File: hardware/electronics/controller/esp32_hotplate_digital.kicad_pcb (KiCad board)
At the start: 2 copper layers, 89.1 x 49.4 mm, 87 parts, among them IC1 ADC081S021CIMF_NOPB, IC2 ADC081S021CIMF_NOPB, J2 JST XH, J3 JST XH, J4 JST XH, J5 JST XH, J6 USB_B_Micro, J7 JST XH, J8 105162-0001, J9 Conn_01x04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

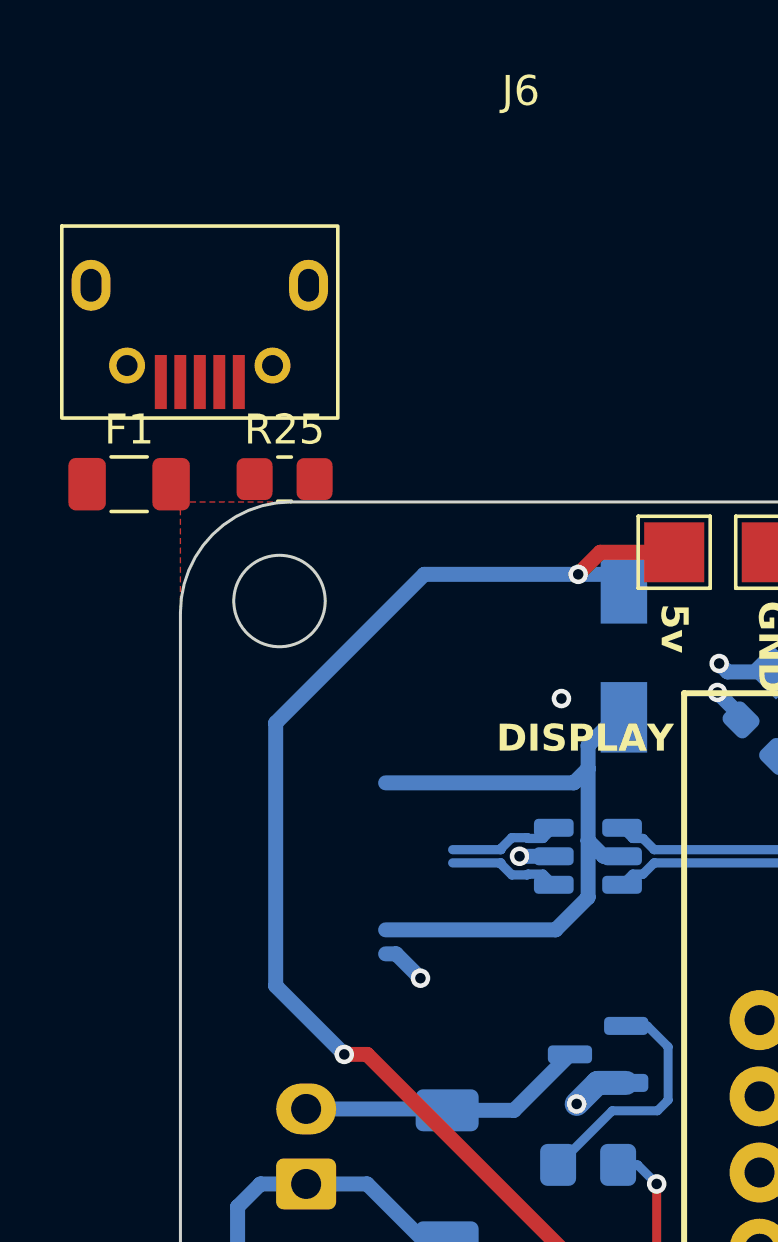
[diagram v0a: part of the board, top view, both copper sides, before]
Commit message: attempting to get the sd card working with SPI
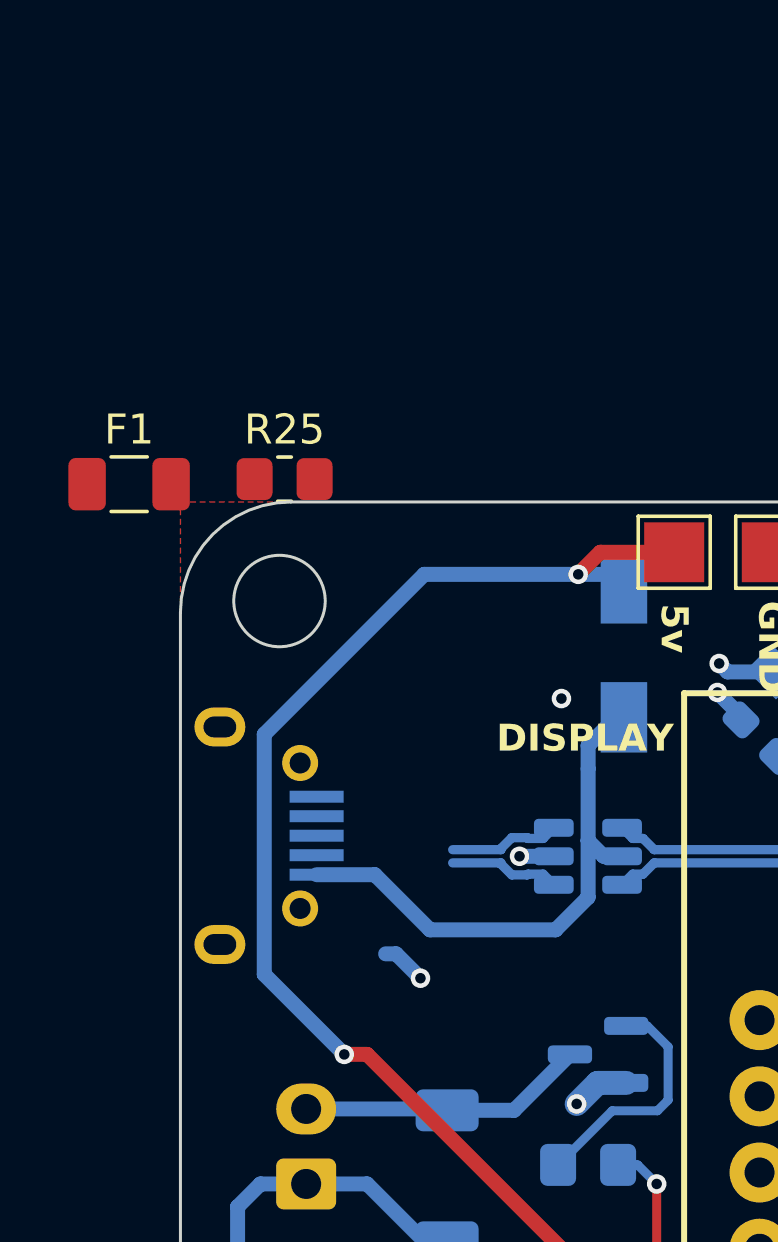
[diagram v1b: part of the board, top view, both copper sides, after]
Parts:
- J6: moved to B.Cu
- moved J6 17.1 mm to (46.2, 62.4), turned to -90 degrees
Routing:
- net VBUS: track 22.0 -> 18.1 mm
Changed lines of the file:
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@@
     )
   )
-  (footprint "Connector_USB:microXNJ" (layer "F.Cu")
-    (at 44.0794 45.511)
-    (property "Sheetfile" "esp32_hotplate_digital.kicad_sch")
-    (property "Sheetname" "")
-    (property "ki_description" "USB Micro Type B connector")
-    (property "ki_keywords" "connector USB micro")
-    (fp_text reference "J6" (at 10.7 -7.9 unlocked) (layer "F.SilkS")
-        (effects (font (size 1 1) (thickness 0.15)))
-    )
-    (fp_text value "USB_B_Micro" (at 10.7 -6.4 unlocked) (layer "F.Fab")
-        (effects (font (size 1 1) (thickness 0.15)))
-    )
-    (fp_text user "${REFERENCE}" (at 10.7 -4.9 unlocked) (layer "F.Fab")
-        (effects (font (size 1 1) (thickness 0.15)))
-    )
-    (fp_rect (start -4.6 -3.4) (end 4.6 3)
-      (stroke (width 0.12) (type default)) (fill none) (layer "F.SilkS"))
-    (fp_rect (start -4.6 -3.4) (end 4.6 3)
-      (stroke (width 0.05) (type default)) (fill none) (layer "F.CrtYd"))
-    (pad "1" smd rect (at 1.3 1.8) (size 0.4 1.8) (layers "F.Cu" "F.Paste" "F.Mask")
-      (net 21 "VBUS") (pinfunction "VBUS") (pintype "power_out"))
-    (pad "2" smd rect (at 0.65 1.8) (size 0.4 1.8) (layers "F.Cu" "F.Paste" "F.Mask")
-      (net 23 "/usb_D-") (pinfunction "D-") (pintype "bidirectional"))
-    (pad "3" smd rect (at 0 1.8) (size 0.4 1.8) (layers "F.Cu" "F.Paste" "F.Mask")
-      (net 22 "/usb_D+") (pinfunction "D+") (pintype "bidirectional"))
-    (pad "4" smd rect (at -0.65 1.8) (size 0.4 1.8) (layers "F.Cu" "F.Paste" "F.Mask")
-      (net 79 "unconnected-(J6-ID-Pad4)") (pinfunction "ID") (pintype "passive"))
-    (pad "5" smd rect (at -1.3 1.8) (size 0.4 1.8) (layers "F.Cu" "F.Paste" "F.Mask")
-      (net 4 "GND") (pinfunction "GND") (pintype "power_out"))
-    (pad "6" thru_hole oval (at -3.625 -1.425) (size 1.3 1.7) (drill oval 0.7 1.1) (layers "*.Cu" "*.Mask")
-      (net 4 "GND") (pinfunction "Shield") (pintype "passive"))
-    (pad "6" thru_hole circle (at -2.425 1.25) (size 1.2 1.2) (drill 0.7) (layers "*.Cu" "*.Mask")
-      (net 4 "GND") (pinfunction "Shield") (pintype "passive"))
-    (pad "6" thru_hole circle (at 2.425 1.25) (size 1.2 1.2) (drill 0.7) (layers "*.Cu" "*.Mask")
-      (net 4 "GND") (pinfunction "Shield") (pintype "passive"))
-    (pad "6" thru_hole oval (at 3.625 -1.425) (size 1.3 1.7) (drill oval 0.7 1.1) (layers "*.Cu" "*.Mask")
-      (net 4 "GND") (pinfunction "Shield") (pintype "passive"))
-  )
   (footprint "TestPoint:TestPoint_Pad_2.0x2.0mm" locked (layer "F.Cu")
     (at 68.58 52.9844 180)
@@
     )
   )
+  (footprint "Connector_USB:microXNJ" (layer "B.Cu")
+    (at 46.173999 62.4332 -90)
+    (property "Sheetfile" "esp32_hotplate_digital.kicad_sch")
+    (property "Sheetname" "")
+    (property "ki_description" "USB Micro Type B connector")
+    (property "ki_keywords" "connector USB micro")
+    (fp_text reference "J6" (at -0.0358 2.4326 90 unlocked) (layer "B.SilkS")
+        (effects (font (size 1 1) (thickness 0.15)) (justify mirror))
+    )
+    (fp_text value "USB_B_Micro" (at 10.7 6.4 90 unlocked) (layer "B.Fab")
+        (effects (font (size 1 1) (thickness 0.15)) (justify mirror))
+    )
+    (fp_text user "${REFERENCE}" (at 10.7 4.9 90 unlocked) (layer "B.Fab")
+        (effects (font (size 1 1) (thickness 0.15)) (justify mirror))
+    )
+    (fp_rect (start -4.6 3.4) (end 4.6 -3)
+      (stroke (width 0.12) (type default)) (fill none) (layer "B.SilkS"))
+    (fp_rect (start -4.6 3.4) (end 4.6 -3)
+      (stroke (width 0.05) (type default)) (fill none) (layer "B.CrtYd"))
+    (pad "1" smd rect (at 1.3 -1.8 270) (size 0.4 1.8) (layers "B.Cu" "B.Paste" "B.Mask")
+      (net 21 "VBUS") (pinfunction "VBUS") (pintype "power_out"))
+    (pad "2" smd rect (at 0.65 -1.8 270) (size 0.4 1.8) (layers "B.Cu" "B.Paste" "B.Mask")
+      (net 23 "/usb_D-") (pinfunction "D-") (pintype "bidirectional"))
+    (pad "3" smd rect (at 0 -1.8 270) (size 0.4 1.8) (layers "B.Cu" "B.Paste" "B.Mask")
+      (net 22 "/usb_D+") (pinfunction "D+") (pintype "bidirectional"))
+    (pad "4" smd rect (at -0.65 -1.8 270) (size 0.4 1.8) (layers "B.Cu" "B.Paste" "B.Mask")
+      (net 79 "unconnected-(J6-ID-Pad4)") (pinfunction "ID") (pintype "passive"))
+    (pad "5" smd rect (at -1.3 -1.8 270) (size 0.4 1.8) (layers "B.Cu" "B.Paste" "B.Mask")
+      (net 4 "GND") (pinfunction "GND") (pintype "power_out"))
+    (pad "6" thru_hole oval (at -3.625 1.425 270) (size 1.3 1.7) (drill oval 0.7 1.1) (layers "*.Cu" "*.Mask")
+      (net 4 "GND") (pinfunction "Shield") (pintype "passive"))
+    (pad "6" thru_hole circle (at -2.425 -1.25 270) (size 1.2 1.2) (drill 0.7) (layers "*.Cu" "*.Mask")
+      (net 4 "GND") (pinfunction "Shield") (pintype "passive"))
+    (pad "6" thru_hole circle (at 2.425 -1.25 270) (size 1.2 1.2) (drill 0.7) (layers "*.Cu" "*.Mask")
+      (net 4 "GND") (pinfunction "Shield") (pintype "passive"))
+    (pad "6" thru_hole oval (at 3.625 1.425 270) (size 1.3 1.7) (drill oval 0.7 1.1) (layers "*.Cu" "*.Mask")
+      (net 4 "GND") (pinfunction "Shield") (pintype "passive"))
+    (model ":KICAD7_3DMODEL_DIR:Connector_USB.3dshapes/USB_Micro-B_Molex_47346-0001.wrl"
+      (offset (xyz 0 0 0))
+      (scale (xyz 1 1 1))
+      (rotate (xyz 0 0 180))
+    )
+  )
   (footprint "Resistor_SMD:R_0805_2012Metric_Pad1.20x1.40mm_HandSolder" (layer "B.Cu")
     (at 57.404 85.598)
@@
   (via (at 48.895 69.723) (size 0.65) (drill 0.35) (layers "F.Cu" "B.Cu") (net 7))
   (via (at 56.6928 53.721) (size 0.65) (drill 0.35) (layers "F.Cu" "B.Cu") (net 7))
-  (segment (start 46.609 58.674) (end 51.562 53.721) (width 0.5) (layer "B.Cu") (net 7))
+  (segment (start 46.228 67.056) (end 46.228 59.055) (width 0.5) (layer "B.Cu") (net 7))
   (segment (start 70.299 97.858) (end 94.912001 97.858) (width 0.5) (layer "B.Cu") (net 7))
   (segment (start 98.790001 93.710001) (end 97.536 92.456) (width 0.5) (layer "B.Cu") (net 7))
   (segment (start 99.06 93.710001) (end 98.790001 93.710001) (width 0.5) (layer "B.Cu") (net 7))
-  (segment (start 46.609 67.437) (end 46.609 58.674) (width 0.5) (layer "B.Cu") (net 7))
   (segment (start 97.536 85.8905) (end 96.4815 84.836) (width 0.5) (layer "B.Cu") (net 7))
   (segment (start 96.4815 84.836) (end 99.2615 82.056) (width 0.5) (layer "B.Cu") (net 7))
+  (segment (start 46.228 59.055) (end 51.562 53.721) (width 0.5) (layer "B.Cu") (net 7))
   (segment (start 56.6928 53.721) (end 57.649 53.721) (width 0.5) (layer "B.Cu") (net 7))
   (segment (start 57.649 53.721) (end 58.039 54.111) (width 0.5) (layer "B.Cu") (net 7))
+  (segment (start 48.895 69.723) (end 46.228 67.056) (width 0.5) (layer "B.Cu") (net 7))
   (segment (start 66.0815 97.075) (end 64.7315 98.425) (width 0.5) (layer "B.Cu") (net 7))
   (segment (start 99.2615 82.056) (end 102.972 82.056) (width 0.5) (layer "B.Cu") (net 7))
   (segment (start 103.6535 82.7375) (end 102.972 82.056) (width 0.5) (layer "B.Cu") (net 7))
   (segment (start 64.659 91.59867) (end 64.659 95.758) (width 0.5) (layer "B.Cu") (net 7))
-  (segment (start 51.562 53.721) (end 56.6928 53.721) (width 0.5) (layer "B.Cu") (net 7))
   (segment (start 69.215 97.075) (end 69.516 97.075) (width 0.5) (layer "B.Cu") (net 7))
-  (segment (start 48.895 69.723) (end 46.609 67.437) (width 0.5) (layer "B.Cu") (net 7))
   (segment (start 97.536 92.456) (end 97.536 85.8905) (width 0.5) (layer "B.Cu") (net 7))
   (segment (start 64.381165 91.320835) (end 64.659 91.59867) (width 0.5) (layer "B.Cu") (net 7))
   (segment (start 69.215 97.075) (end 66.0815 97.075) (width 0.5) (layer "B.Cu") (net 7))
   (segment (start 69.516 97.075) (end 70.299 97.858) (width 0.5) (layer "B.Cu") (net 7))
+  (segment (start 51.562 53.721) (end 56.6928 53.721) (width 0.5) (layer "B.Cu") (net 7))
   (segment (start 103.6535 84.836) (end 103.6535 82.7375) (width 0.5) (layer "B.Cu") (net 7))
   (segment (start 94.912001 97.858) (end 99.06 93.710001) (width 0.5) (layer "B.Cu") (net 7))
@@
   (segment (start 98.407328 68.366) (end 115.916 68.366) (width 0.3) (layer "B.Cu") (net 20))
   (segment (start 73.914 74.676) (end 73.914 73.146) (width 0.3) (layer "B.Cu") (net 20))
-  (segment (start 50.273 60.671) (end 56.55 60.671) (width 0.5) (layer "B.Cu") (net 21))
-  (segment (start 56.55 60.671) (end 57.023 60.198) (width 0.5) (layer "B.Cu") (net 21))
   (segment (start 58.155 63.119) (end 57.543972 63.119) (width 0.5) (layer "B.Cu") (net 21))
   (segment (start 57.023 60.198) (end 57.023 59.427) (width 0.5) (layer "B.Cu") (net 21))
   (segment (start 57.023 59.427) (end 58.039 58.411) (width 0.5) (layer "B.Cu") (net 21))
-  (segment (start 50.273 65.571) (end 55.939028 65.571) (width 0.5) (layer "B.Cu") (net 21))
-  (segment (start 57.023 64.487028) (end 57.023 62.598028) (width 0.5) (layer "B.Cu") (net 21))
+  (segment (start 57.023 62.598028) (end 57.023 64.487028) (width 0.5) (layer "B.Cu") (net 21))
+  (segment (start 57.023 64.487028) (end 55.939028 65.571) (width 0.5) (layer "B.Cu") (net 21))
+  (segment (start 49.9156 63.7332) (end 47.973999 63.7332) (width 0.5) (layer "B.Cu") (net 21))
   (segment (start 57.023 62.598028) (end 57.023 60.198) (width 0.5) (layer "B.Cu") (net 21))
-  (segment (start 55.939028 65.571) (end 57.023 64.487028) (width 0.5) (layer "B.Cu") (net 21))
   (segment (start 57.543972 63.119) (end 57.023 62.598028) (width 0.5) (layer "B.Cu") (net 21))
+  (segment (start 55.939028 65.571) (end 51.7534 65.571) (width 0.5) (layer "B.Cu") (net 21))
+  (segment (start 51.7534 65.571) (end 49.9156 63.7332) (width 0.5) (layer "B.Cu") (net 21))
   (segment (start 54.480187 63.739) (end 54.117 63.375813) (width 0.31) (layer "B.Cu") (net 22))
   (segment (start 54.117 63.375813) (end 54.117 63.339) (width 0.31) (layer "B.Cu") (net 22))

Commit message: fixes for revision2
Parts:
- removed J6: USB_B_Micro, Connector_USB:microXNJ
- added F2: 1A, Fuse:Fuse_1206_3216Metric, F.Cu at (39.6, 94.2)
- added J1: USB_C_Receptacle_USB2.0, Connector_USB:USB_C_Receptacle_HRO_TYPE-C-31-M-12, B.Cu at (46.2, 63.1)
- added R26: 10k, Resistor_SMD:R_0805_2012Metric_Pad1.20x1.40mm_HandSolder, B.Cu at (125.1, 108.4)
- added R27: 10k, Resistor_SMD:R_0805_2012Metric_Pad1.20x1.40mm_HandSolder, B.Cu at (125.1, 111.4)
- added R5: 10k, Resistor_SMD:R_0805_2012Metric_Pad1.20x1.40mm_HandSolder, F.Cu at (17.8, 67.9)
- added R6: 10k, Resistor_SMD:R_0805_2012Metric_Pad1.20x1.40mm_HandSolder, F.Cu at (17.8, 70.9)
- F1: value Fuse -> 1A
- J8: footprint SamacSys_Parts:105162-0001 -> components:TF-SMD_TF-PUSH
- R25: moved to B.Cu
- moved R25 93.9 mm to (116.6, 113.4), turned to 180 degrees
- moved R23 22.7 mm to (109.1, 70.9), turned to -90 degrees
- moved R24 19.1 mm to (111.3, 72.1), turned to -90 degrees
- moved J8 5.20 mm to (122.7, 84.7)
- moved BZ1 2.78 mm to (109.5, 80.4)
- moved R22 2.29 mm to (122.8, 73.5)
- moved R21 1.93 mm to (122.8, 75.6)
- moved R11 1.37 mm to (105.7, 74.5), turned to 0 degrees
- turned SW3 to 0 degrees
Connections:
- J7 pad 2: +12V -> Net-(J7-Pin_2)
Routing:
- net /HSPI_MOSI: track 95.8 -> 70.2 mm
- net /SD_CS: track 92.5 -> 68.1 mm
- net GND: track 87.9 -> 102.9 mm, vias 37 -> 38
- net +3.3V: track 233.1 -> 247.6 mm, vias 5 -> 6
- net /BTN_DOWN: track 66.3 -> 60.8 mm
- net Net-(R10-Pad2): track 60.6 -> 65.7 mm
- net /usb_D-: track 3.72 -> 0.00 mm
- net /usb_D+: track 3.72 -> 0.00 mm
- net VBUS: track 18.1 -> 15.0 mm
- net /HSPI_MISO: track 82.8 -> 80.0 mm
- net /HEATER: track 39.6 -> 41.9 mm
- net /ZERO_CROSS: track 35.5 -> 37.1 mm
- net /HSPI_CLK: track 81.7 -> 83.2 mm
- net /EN: track 54.1 -> 53.5 mm, vias 4 -> 2
- net /DISP_DC: track 27.0 -> 27.5 mm
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
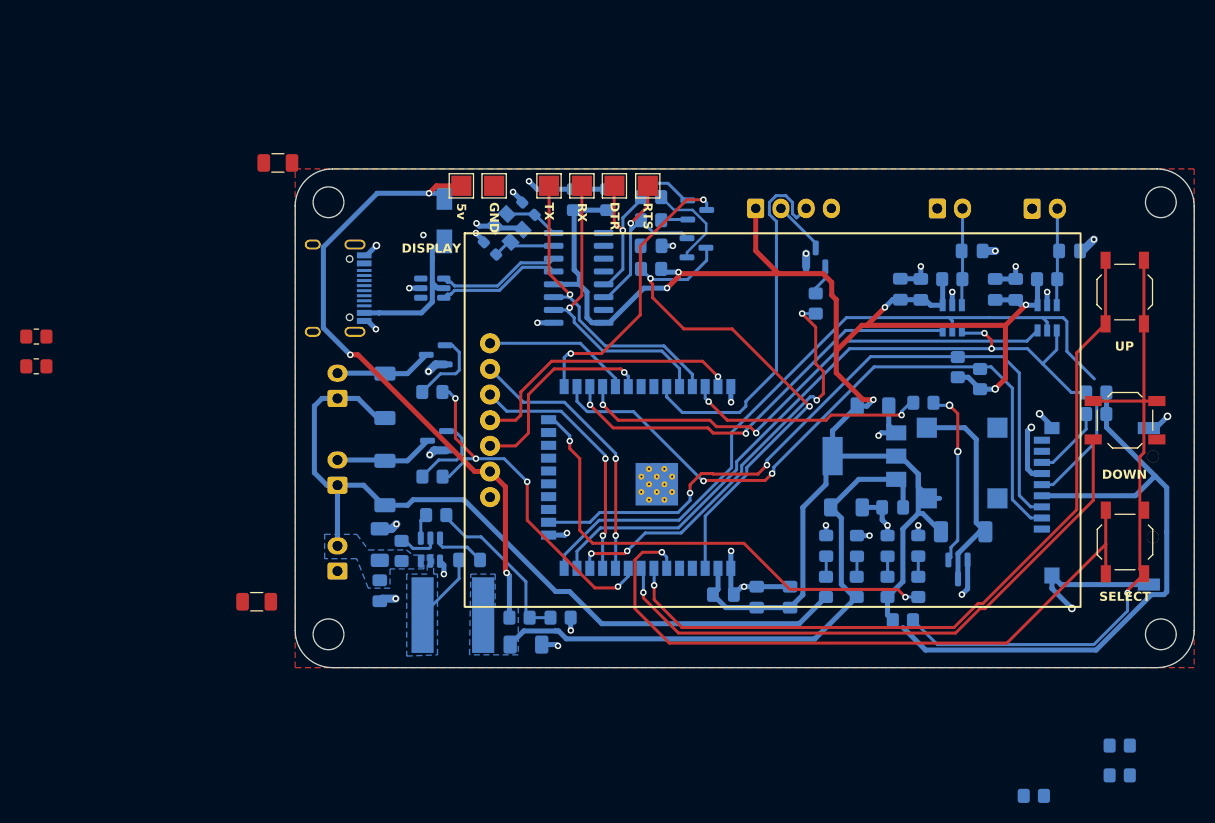
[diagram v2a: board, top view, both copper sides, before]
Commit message: controller can now draw reflow profiles from the sd card, if no card is available a default profile will be loaded
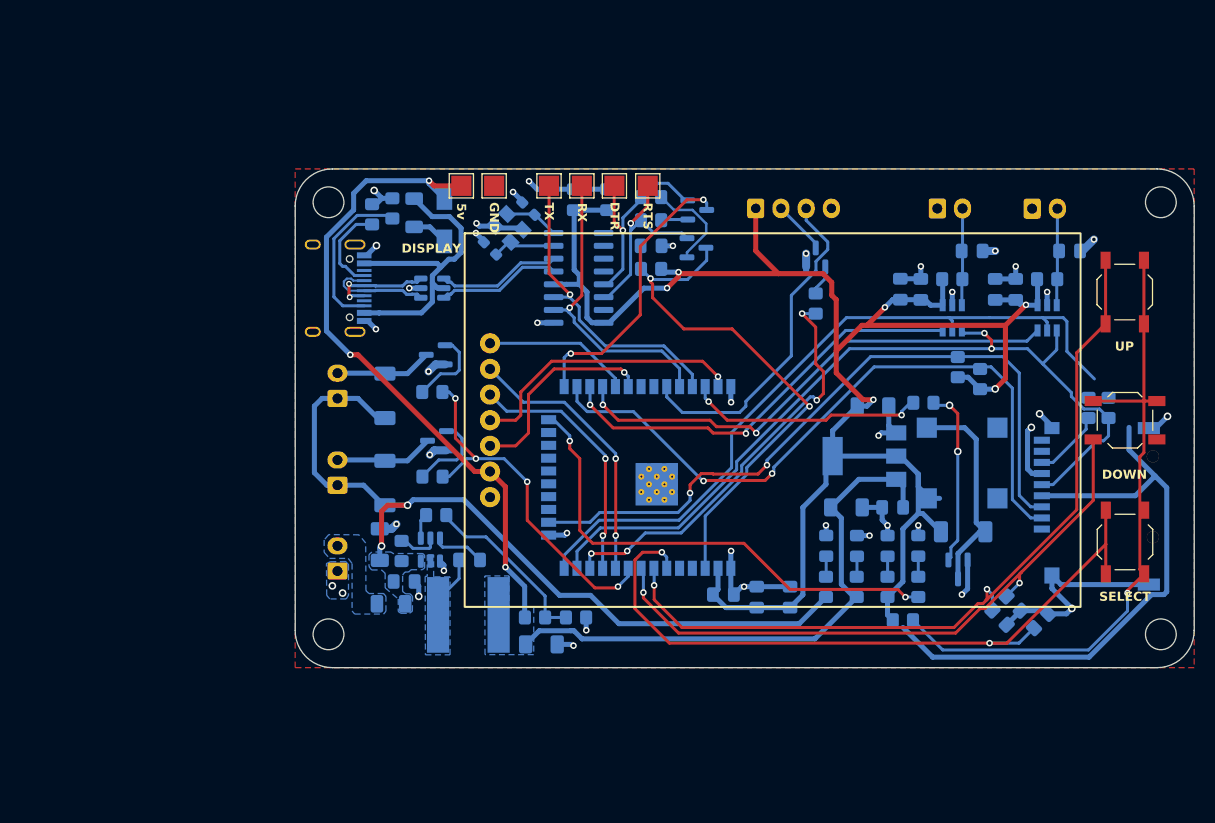
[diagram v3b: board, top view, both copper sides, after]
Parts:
- F1, F2, R5, R6: moved to B.Cu
- moved R5 37.5 mm to (53.1, 55.2), turned to -90 degrees
- moved R6 36.5 mm to (51.1, 55.8), turned to -90 degrees
- moved R27 19.6 mm to (113.2, 95.8), turned to 135 degrees
- moved R26 17.6 mm to (114.6, 94.4), turned to 135 degrees
- moved R25 17.3 mm to (117.3, 96.1), turned to -135 degrees
- moved F1 14.4 mm to (55.2, 55.7), turned to -90 degrees
- moved F2 13.3 mm to (52.9, 94.4)
- moved C2 2.58 mm to (54.2, 92.2), turned to 0 degrees
- moved R22 1.95 mm to (124.0, 75.0), turned to 90 degrees
- moved C4 1.53 mm to (67.8, 98.4)
- moved R4 1.53 mm to (71.3, 95.7)
- moved L1 1.53 mm to (60.6, 95.5)
- moved R3 1.53 mm to (67.2, 95.7)
- moved R21 0.98 mm to (122.0, 75.0), turned to 90 degrees
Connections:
- R6 pad 1: unconnected-(R6-Pad1) -> GND
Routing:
- net Net-(J1-SBU2): track 0.00 -> 16.0 mm
- net VBUS: track 15.0 -> 31.0 mm
- net /usb_D+: track 0.00 -> 10.8 mm
- net /usb_D-: track 0.00 -> 10.4 mm, vias 0 -> 2
- net GND: track 102.9 -> 113.2 mm, vias 38 -> 40
- net Net-(J1-SBU1): track 0.00 -> 9.04 mm
- net /BTN_SELECT: track 67.8 -> 72.8 mm, vias 1 -> 2
- net /ZERO_CROSS: track 37.1 -> 33.3 mm
- net Net-(D9-A): track 0.00 -> 3.59 mm
- net +3.3V: track 247.6 -> 244.0 mm
- net /BTN_UP: track 77.1 -> 80.6 mm, vias 1 -> 2
- net /BTN_DOWN: track 60.8 -> 63.8 mm, vias 1 -> 2
- net +12V: track 79.1 -> 80.9 mm, vias 0 -> 2
- net Net-(R2-Pad2): track 16.5 -> 18.0 mm
- net /HSPI_CLK: track 83.2 -> 84.6 mm
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- added copper zone on B.Cu, net GND
- added copper zone on B.Cu, net Net-(J7-Pin_2)
